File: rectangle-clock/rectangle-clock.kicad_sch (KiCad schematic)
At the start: 40 parts

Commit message: update
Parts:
- added BT1: Battery_Cell, footprints:BatteryHolder_Keystone_106_1x20mm, symbol HPS:Battery_Cell
- gave numbers to parts that had none: 36
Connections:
- net DIG6: now also DS2.10 (COM_DIG.3); no longer DS2.14 (COM_DIG.1)
- net DIG7: now also DS2.6 (COM_DIG.4); no longer DS2.11 (COM_DIG.2)
- net GND: now also R6.2, SW2.4 (B), SW3.4 (B), SW4.4 (B), BT1.2 (-); no longer R7.2, U1.23 (PC0), U1.24 (PC1), U1.25 (PC2)
- net PHR: now also R6.1, R7.2; no longer R6.2, R7.1
- net VCC: now also R7.1; no longer R6.1
- net B3: now reaches R12.2, SW4.1 (A)
- net B3: now also SW4.2 (A), U1.23 (PC0)
- net B2: now reaches R9.2, SW3.1 (A)
- net B2: now also SW3.2 (A), U1.24 (PC1)
- net B1: now reaches R8.2, SW2.1 (A)
- net B1: now also SW2.2 (A), U1.25 (PC2)
- net +BATT: no longer names the net of U4.3 (VBAT)
- net +BATT: now also BT1.1 (+)
- net COLON: no longer names the net of DS1.7 (COM_COLON)
- net COLON: no longer U3.3 (DIG_4)
- net COLON2: no longer names the net of DS1.8 (COLON)
- net COLON2: no longer U3.10 (DIG_5)
- new net DIG4: DS2.14 (COM_DIG.1), U3.3 (DIG_4)
- new net DIG5: DS2.11 (COM_DIG.2), U3.10 (DIG_5)
- no-connect marks 2 -> 4
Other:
- moved on the sheet: H1, H2, H3, H4, R6, R7

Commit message: initial gerber out
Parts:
- removed J1: PJ-102AH, footprints:PJ-102AH, symbol HPS:PJ-102AH
- removed U2: L7805_TO92, footprints:TO-92_Inline, symbol HPS:L7805_TO92
- added J2: Power_inlet_vertical, footprints:Wurth-694106402002, symbol HPS:Power_inlet_vertical
- added U2: L7805, footprints:TO-252-2, symbol HPS:L7805
- C3, C4: value C_22pf -> C_0805_22pf
- C6: value C_0.1uf -> C_0805_0.1uf
- R1, R3, R4: value R_10K -> R_0805_10K
- R13: value R_2.2K -> R_0805_2.2K
- renumbered DS2 to DS1, DS1 to DS2, J3 to J1, J2 to J3, R7 to R6, R6 to R7, U4 to U1, U1 to U3, U3 to U4, Y2 to Y1, Y1 to Y2
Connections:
- net GND: now also J2.2 (OUT), U2.2 (GND)
- net VCC: now also U2.3 (OUT)
- net at C5.1: now also J2.1 (POLE), U2.1 (IN)
- no-connect marks 4 -> 5

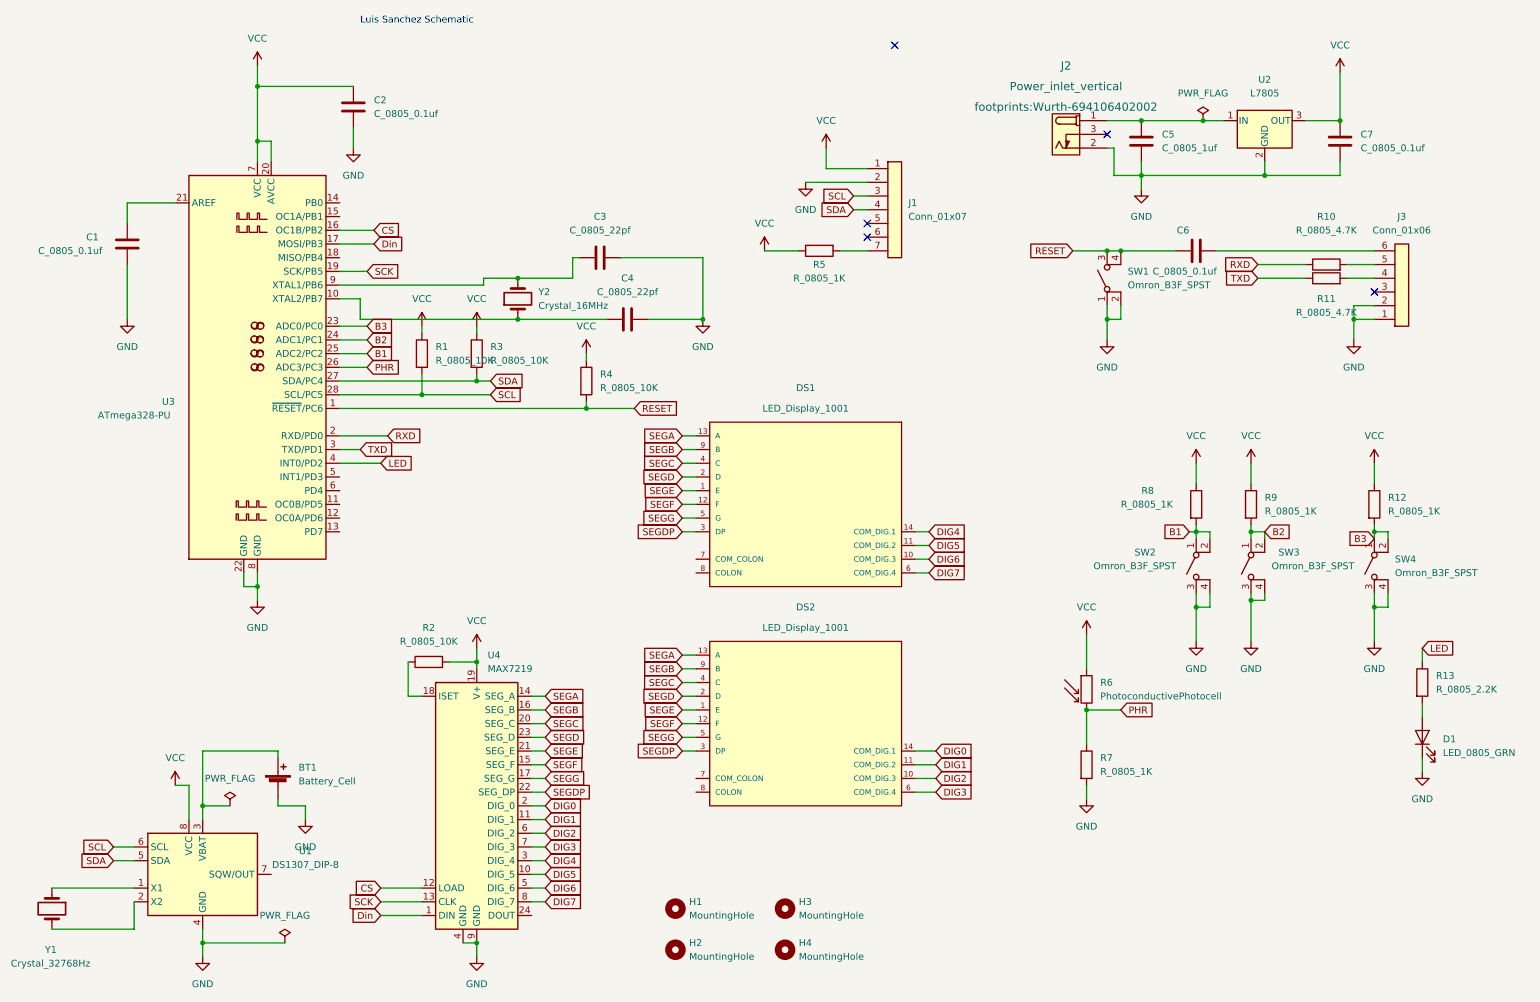
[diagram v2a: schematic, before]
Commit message: Added Test points
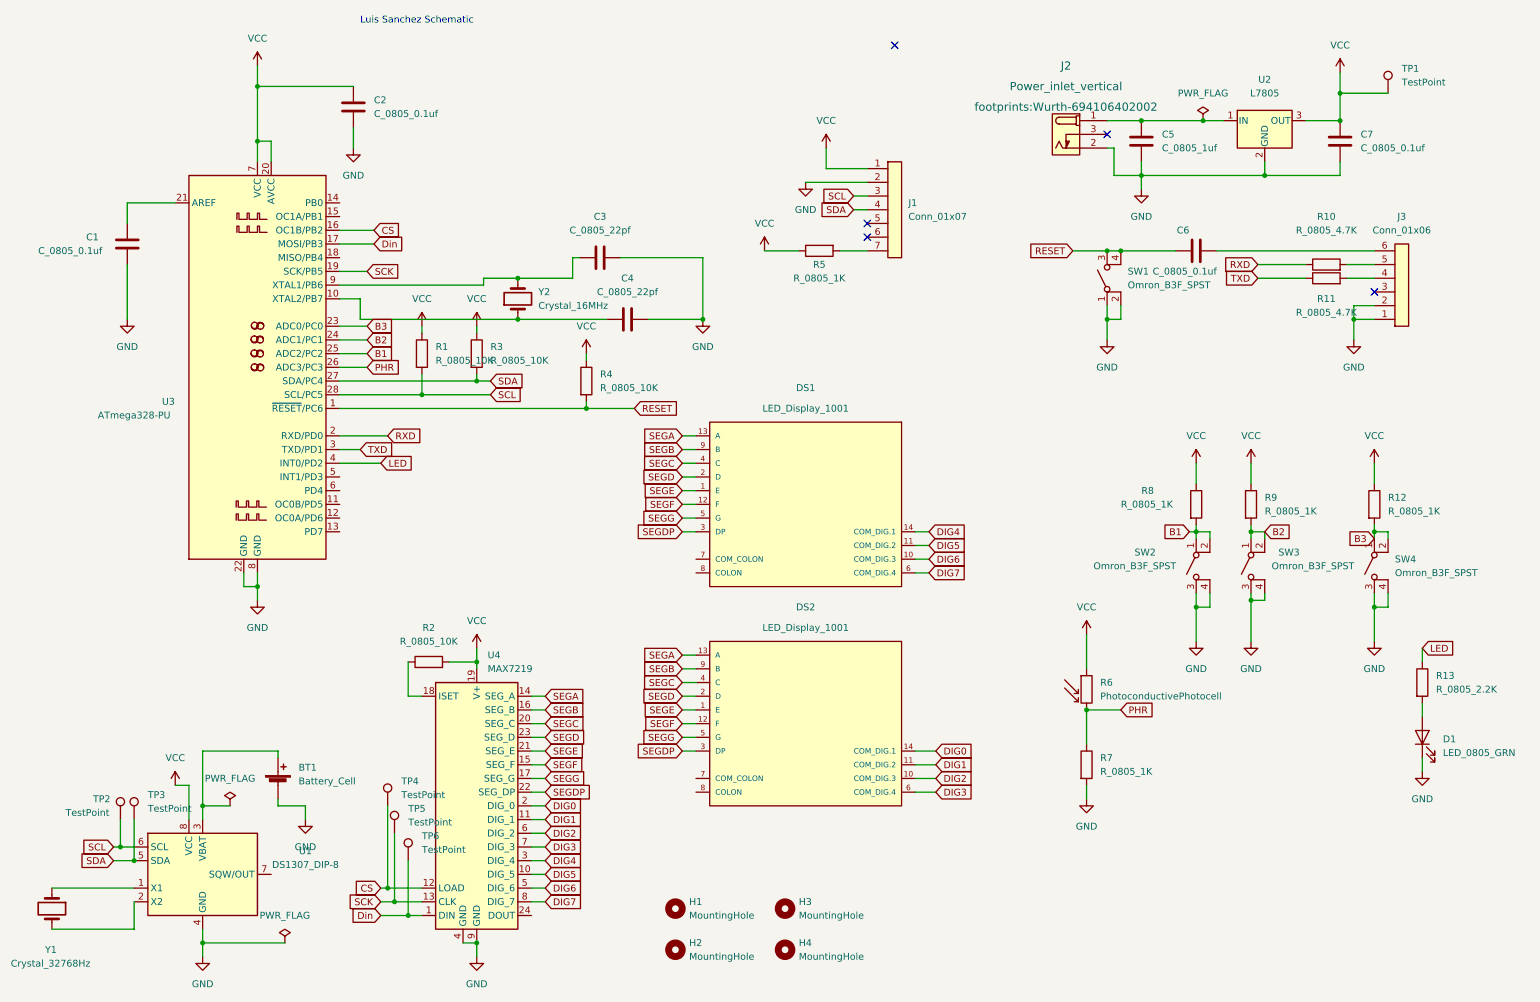
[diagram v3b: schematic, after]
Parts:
- added TP1, TP2, TP3, TP4, TP5, TP6: TestPoint, footprints:TestPoint_THTPad_D2.0mm_Drill1.0mm, symbol HPS:TestPoint
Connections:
- net CS: now also TP4.1
- net Din: now also TP6.1
- net SCK: now also TP5.1
- net SCL: now also TP2.1
- net SDA: now also TP3.1
- net VCC: now also TP1.1

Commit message: Final gerber commit
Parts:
- removed R5: R_0805_1K, footprints:R_0805_2012Metric, symbol HPS:R_0805_1K
- added R5: R_0805_10K, footprints:R_0805_2012Metric, symbol HPS:R_0805_10K
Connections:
- net VCC: now also R5.1
- net at J1.7 (Pin_7): now also R5.2
- no-connect marks 5 -> 4
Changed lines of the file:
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@@
   )
   (no_connect (at 215.9 39.37))
-  (no_connect (at 176.53 22.86))
   (no_connect (at 265.43 68.58))
   (no_connect (at 171.45 58.42))
@@
     (pin "1")
   )
+  (symbol (lib_id "HPS:R_0805_10K") (at 162.56 60.96 90) (unit 1)
+    (in_bom yes) (on_board yes) (fields_autoplaced)
+    (property "Reference" "R5" (id 0) (at 162.56 54.61 90))
+    (property "Value" "R_0805_10K" (id 1) (at 162.56 57.15 90))
+    (property "Footprint" "footprints:R_0805_2012Metric" (id 2) (at 179.07 60.96 0)
+      (effects (font (size 1.27 1.27)) hide)
+    )
+    (property "Datasheet" "https://www.digikey.com/en/products/detail/yageo/RC0805FR-0710KL/727535" (id 3) (at 162.56 63.5 0)
+      (effects (font (size 1.27 1.27)) hide)
+    )
+    (property "MFG" "Yageo" (id 4) (at 173.99 60.96 0)
+      (effects (font (size 1.27 1.27)) hide)
+    )
+    (property "MPN" "RC0805FR-0710KL" (id 5) (at 176.53 60.96 0)
+      (effects (font (size 1.27 1.27)) hide)
+    )
+    (property "Digikey PN" "311-10.0KCRCT-ND" (id 6) (at 181.61 60.96 0)
+      (effects (font (size 1.27 1.27)) hide)
+    )
+    (property "Mouser PN" "N/A" (id 7) (at 184.15 60.96 0)
+      (effects (font (size 1.27 1.27)) hide)
+    )
+    (property "Power" "N/A" (id 8) (at 186.69 60.96 0)
+      (effects (font (size 1.27 1.27)) hide)
+    )
+    (property "Tolerance" "N/A" (id 9) (at 189.23 60.96 0)
+      (effects (font (size 1.27 1.27)) hide)
+    )
+    (pin "1")
+    (pin "2")
+  )
   (symbol (lib_id "HPS:MAX7219") (at 99.06 163.83 0) (unit 1)
     (in_bom yes) (on_board yes) (fields_autoplaced)
@@
     (pin "1")
   )
-  (symbol (lib_id "HPS:R_0805_1K") (at 162.56 60.96 90) (mirror x) (unit 1)
-    (in_bom yes) (on_board yes)
-    (property "Reference" "R5" (id 0) (at 162.56 63.5 90))
-    (property "Value" "R_0805_1K" (id 1) (at 162.56 66.04 90))
-    (property "Footprint" "footprints:R_0805_2012Metric" (id 2) (at 179.07 60.96 0)
-      (effects (font (size 1.27 1.27)) hide)
-    )
-    (property "Datasheet" "https://www.digikey.com/en/products/detail/yageo/RC0805FR-071KL/727444" (id 3) (at 162.56 58.42 0)
-      (effects (font (size 1.27 1.27)) hide)
-    )
-    (property "MFG" "Yageo" (id 4) (at 173.99 60.96 0)
-      (effects (font (size 1.27 1.27)) hide)
-    )
-    (property "Digikey PN" "RC0805FR-0710KL" (id 5) (at 176.53 60.96 0)
-      (effects (font (size 1.27 1.27)) hide)
-    )
-    (property "Mouser PN" "N/A" (id 6) (at 189.23 60.96 0)
-      (effects (font (size 1.27 1.27)) hide)
-    )
-    (property "Power" "N/A" (id 7) (at 186.69 60.96 0)
-      (effects (font (size 1.27 1.27)) hide)
-    )
-    (property "Tolerance" "N/A" (id 8) (at 184.15 60.96 0)
-      (effects (font (size 1.27 1.27)) hide)
-    )
-    (property "MPN" "RC0805FR-071KL" (id 9) (at 181.61 60.96 0)
-      (effects (font (size 1.27 1.27)) hide)
-    )
-    (pin "1")
-    (pin "2")
-  )
   (symbol (lib_id "HPS:GND") (at 242.57 133.35 0) (unit 1)
     (in_bom yes) (on_board yes) (fields_autoplaced)
@@
       (reference "R4") (unit 1) (value "R_0805_10K") (footprint "footprints:R_0805_2012Metric")
     )
-    (path "/bafe5572-5eb7-405d-869f-a7a05b2e7e1a"
-      (reference "R5") (unit 1) (value "R_0805_1K") (footprint "footprints:R_0805_2012Metric")
+    (path "/94b81966-c211-4bd0-bca7-65c3513d05d7"
+      (reference "R5") (unit 1) (value "R_0805_10K") (footprint "footprints:R_0805_2012Metric")
     )
     (path "/af10ac51-346f-4803-be83-fe22e5579112"

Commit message: Revised Board/Final Gerber out
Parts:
- removed R1, R2, R3: R_0805_10K, footprints:R_0805_2012Metric, symbol HPS:R_0805_10K
- removed R12, R7, R8, R9: R_0805_1K, footprints:R_0805_2012Metric, symbol HPS:R_0805_1K
- added C8: C_0805_10uf, footprints:C_0805_2012Metric, symbol HPS:C_0805_10uf
- added C9: C_0805_0.1uf, footprints:C_0805_2012Metric, symbol HPS:C_0805_0.1uf
- added J4: Conn_02x03_Odd_Even, footprints:PinHeader_2x03_P2.54mm_Vertical, symbol HPS:Conn_02x03_Odd_Even
- added R1, R3: R_0805_4.7K, footprints:R_0805_2012Metric, symbol HPS:R_0805_4.7K
- added R12, R8, R9: R_0805_10K, footprints:R_0805_2012Metric, symbol HPS:R_0805_10K
- added R2: R_0805_22K, footprints:R_0805_2012Metric, symbol HPS:R_0805_22K
- added R7: R_0805_100K, footprints:R_0805_2012Metric, symbol HPS:R_0805_100K
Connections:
- net B1: now also R8.2
- net B2: now also R9.2
- net B3: now also R12.2
- net Din: now also J4.2 (Pin_2)
- net GND: now also C8.2, C9.2, J4.3 (Pin_3), R7.2
- net PHR: now also R7.1
- net RESET: now also J4.5 (Pin_5)
- net SCK: now also R13.1, J4.6 (Pin_6)
- net SCL: now also R1.2
- net SDA: now also R3.2
- net VCC: now also C8.1, C9.1, J4.1 (Pin_1), R1.1, R12.1, R2.2, R3.1, R8.1, R9.1
- net at U4.18 (ISET): now also R2.1
- net MISO: now reaches U3.18 (MISO/PB4)
- net MISO: now also J4.4 (Pin_4)
- net LED: no longer names the net of U3.4 (INT0/PD2)
- net LED: no longer R13.1
- no-connect marks 4 -> 18
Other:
- note added: "Connection to accelerometer"

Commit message: Final push? :)
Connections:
- net Din: now also J4.4 (Pin_4); no longer J4.2 (Pin_2)
- net GND: now also J4.6 (Pin_6); no longer J4.3 (Pin_3)
- net MISO: now also J4.1 (Pin_1); no longer J4.4 (Pin_4)
- net SCK: now also J4.3 (Pin_3); no longer J4.6 (Pin_6)
- net VCC: now also J4.2 (Pin_2); no longer J4.1 (Pin_1)
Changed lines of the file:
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@@
+    (stroke (width 0) (type default) (color 0 0 0 0))
+  )
+  (wire (pts (xy 144.78 31.75) (xy 138.43 31.75))
     (stroke (width 0) (type default) (color 0 0 0 0))
   )
@@
     (stroke (width 0) (type default) (color 0 0 0 0))
   )
+  (wire (pts (xy 123.19 36.83) (xy 125.73 36.83))
+    (stroke (width 0) (type default) (color 0 0 0 0))
+  )
   (wire (pts (xy 73.66 90.17) (xy 119.38 90.17))
     (stroke (width 0) (type default) (color 0 0 0 0))
@@
     (stroke (width 0) (type default) (color 0 0 0 0))
   )
-  (wire (pts (xy 139.7 31.75) (xy 138.43 31.75))
-    (stroke (width 0) (type default) (color 0 0 0 0))
-  )
   (wire (pts (xy 125.73 62.23) (xy 140.97 62.23))
     (stroke (width 0) (type default) (color 0 0 0 0))
@@
     (stroke (width 0) (type default) (color 0 0 0 0))
   )
-  (wire (pts (xy 115.57 31.75) (xy 125.73 31.75))
+  (wire (pts (xy 139.7 36.83) (xy 138.43 36.83))
     (stroke (width 0) (type default) (color 0 0 0 0))
   )
@@
     (stroke (width 0) (type default) (color 0 0 0 0))
   )
-  (wire (pts (xy 114.3 34.29) (xy 125.73 34.29))
-    (stroke (width 0) (type default) (color 0 0 0 0))
-  )
   (wire (pts (xy 215.9 73.66) (xy 215.9 77.47))
     (stroke (width 0) (type default) (color 0 0 0 0))
@@
     (stroke (width 0) (type default) (color 0 0 0 0))
   )
+  (wire (pts (xy 140.97 34.29) (xy 138.43 34.29))
+    (stroke (width 0) (type default) (color 0 0 0 0))
+  )
   (wire (pts (xy 76.2 38.1) (xy 76.2 41.91))
     (stroke (width 0) (type default) (color 0 0 0 0))
@@
     (stroke (width 0) (type default) (color 0 0 0 0))
   )
-  (wire (pts (xy 139.7 36.83) (xy 138.43 36.83))
-    (stroke (width 0) (type default) (color 0 0 0 0))
-  )
-  (wire (pts (xy 139.7 34.29) (xy 138.43 34.29))
-    (stroke (width 0) (type default) (color 0 0 0 0))
-  )
   (wire (pts (xy 265.43 113.03) (xy 267.97 113.03))
     (stroke (width 0) (type default) (color 0 0 0 0))
@@
     (stroke (width 0) (type default) (color 0 0 0 0))
   )
+  (wire (pts (xy 123.19 31.75) (xy 125.73 31.75))
+    (stroke (width 0) (type default) (color 0 0 0 0))
+  )
+  (wire (pts (xy 123.19 34.29) (xy 125.73 34.29))
+    (stroke (width 0) (type default) (color 0 0 0 0))
+  )
   (wire (pts (xy 212.09 138.43) (xy 212.09 132.08))
     (stroke (width 0) (type default) (color 0 0 0 0))
@@
     (stroke (width 0) (type default) (color 0 0 0 0))
   )
+  (wire (pts (xy 144.78 25.4) (xy 144.78 31.75))
+    (stroke (width 0) (type default) (color 0 0 0 0))
+  )
   (wire (pts (xy 83.82 168.91) (xy 83.82 181.61))
     (stroke (width 0) (type default) (color 0 0 0 0))
@@
   )
   (wire (pts (xy 58.42 26.67) (xy 58.42 30.48))
+    (stroke (width 0) (type default) (color 0 0 0 0))
+  )
+  (wire (pts (xy 139.7 43.18) (xy 139.7 36.83))
     (stroke (width 0) (type default) (color 0 0 0 0))
   )
@@
     )
   )
-  (global_label "MISO" (shape input) (at 139.7 34.29 0) (fields_autoplaced)
-    (effects (font (size 1.27 1.27)) (justify left))
-    (property "Intersheet References" "${INTERSHEET_REFS}" (id 0) (at 146.7093 34.2106 0)
-      (effects (font (size 1.27 1.27)) (justify left) hide)
+  (global_label "MISO" (shape input) (at 123.19 31.75 180) (fields_autoplaced)
+    (effects (font (size 1.27 1.27)) (justify right))
+    (property "Intersheet References" "${INTERSHEET_REFS}" (id 0) (at 116.1807 31.6706 0)
+      (effects (font (size 1.27 1.27)) (justify right) hide)
     )
   )
@@
     )
   )
-  (global_label "RESET" (shape input) (at 125.73 36.83 180) (fields_autoplaced)
-    (effects (font (size 1.27 1.27)) (justify right))
-    (property "Intersheet References" "${INTERSHEET_REFS}" (id 0) (at 117.5717 36.7506 0)
+  (global_label "RESET" (shape input) (at 123.19 36.83 180) (fields_autoplaced)
+    (effects (font (size 1.27 1.27)) (justify right))
+    (property "Intersheet References" "${INTERSHEET_REFS}" (id 0) (at 115.0317 36.7506 0)
       (effects (font (size 1.27 1.27)) (justify right) hide)
     )
@@
     )
   )
-  (global_label "SCK" (shape input) (at 139.7 36.83 0) (fields_autoplaced)
-    (effects (font (size 1.27 1.27)) (justify left))
-    (property "Intersheet References" "${INTERSHEET_REFS}" (id 0) (at 145.8626 36.7506 0)
-      (effects (font (size 1.27 1.27)) (justify left) hide)
+  (global_label "SCK" (shape input) (at 123.19 34.29 180) (fields_autoplaced)
+    (effects (font (size 1.27 1.27)) (justify right))
+    (property "Intersheet References" "${INTERSHEET_REFS}" (id 0) (at 117.0274 34.2106 0)
+      (effects (font (size 1.27 1.27)) (justify right) hide)
     )
   )
@@
     )
   )
-  (global_label "Din" (shape input) (at 139.7 31.75 0) (fields_autoplaced)
-    (effects (font (size 1.27 1.27)) (justify left))
-    (property "Intersheet References" "${INTERSHEET_REFS}" (id 0) (at 145.1369 31.6706 0)
+  (global_label "Din" (shape input) (at 140.97 34.29 0) (fields_autoplaced)
+    (effects (font (size 1.27 1.27)) (justify left))
+    (property "Intersheet References" "${INTERSHEET_REFS}" (id 0) (at 146.4069 34.2106 0)
       (effects (font (size 1.27 1.27)) (justify left) hide)
     )
@@
     (pin "2")
   )
-  (symbol (lib_id "HPS:VCC") (at 115.57 31.75 0) (unit 1)
-    (in_bom yes) (on_board yes) (fields_autoplaced)
-    (property "Reference" "#PWR0134" (id 0) (at 115.57 35.56 0)
-      (effects (font (size 1.27 1.27)) hide)
-    )
-    (property "Value" "VCC" (id 1) (at 115.57 26.67 0))
-    (property "Footprint" "" (id 2) (at 115.57 31.75 0)
-      (effects (font (size 1.27 1.27)) hide)
-    )
-    (property "Datasheet" "" (id 3) (at 115.57 31.75 0)
+  (symbol (lib_id "HPS:VCC") (at 144.78 25.4 0) (unit 1)
+    (in_bom yes) (on_board yes) (fields_autoplaced)
+    (property "Reference" "#PWR0134" (id 0) (at 144.78 29.21 0)
+      (effects (font (size 1.27 1.27)) hide)
+    )
+    (property "Value" "VCC" (id 1) (at 144.78 20.32 0))
+    (property "Footprint" "" (id 2) (at 144.78 25.4 0)
+      (effects (font (size 1.27 1.27)) hide)
+    )
+    (property "Datasheet" "" (id 3) (at 144.78 25.4 0)
       (effects (font (size 1.27 1.27)) hide)
     )
@@
     (pin "1")
   )
-  (symbol (lib_id "HPS:GND") (at 114.3 34.29 0) (unit 1)
-    (in_bom yes) (on_board yes) (fields_autoplaced)
-    (property "Reference" "#PWR0133" (id 0) (at 114.3 40.64 0)
-      (effects (font (size 1.27 1.27)) hide)
-    )
-    (property "Value" "GND" (id 1) (at 114.3 39.37 0))
-    (property "Footprint" "" (id 2) (at 114.3 34.29 0)
-      (effects (font (size 1.27 1.27)) hide)
-    )
-    (property "Datasheet" "" (id 3) (at 114.3 34.29 0)
-      (effects (font (size 1.27 1.27)) hide)
-    )
+  (symbol (lib_id "HPS:GND") (at 139.7 43.18 0) (unit 1)
+    (in_bom yes) (on_board yes) (fields_autoplaced)
+    (property "Reference" "#PWR0133" (id 0) (at 139.7 49.53 0)
+      (effects (font (size 1.27 1.27)) hide)
+    )
+    (property "Value" "GND" (id 1) (at 139.7 48.26 0))
+    (property "Footprint" "" (id 2) (at 139.7 43.18 0)
+      (effects (font (size 1.27 1.27)) hide)
+    )
+    (property "Datasheet" "" (id 3) (at 139.7 43.18 0)
+      (effects (font (size 1.27 1.27)) hide)
+    )
